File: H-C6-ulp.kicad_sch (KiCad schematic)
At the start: 66 parts, among them J1 USB_C_Receptacle_USB2.0, J2 AFC24-S24FIC-00, J3 SM02B-SRSS-TB(LF)(SN), J4 SM04B-SRSS-TB_LF__SN_, Q1 Si1308, Q2 Si2301CDS, U1 ESP32-C6, U2 SGM6029CYG/TR, U3 TP4057-42-SOT26-R, X1 Crystal 40 Mhz 10ppm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

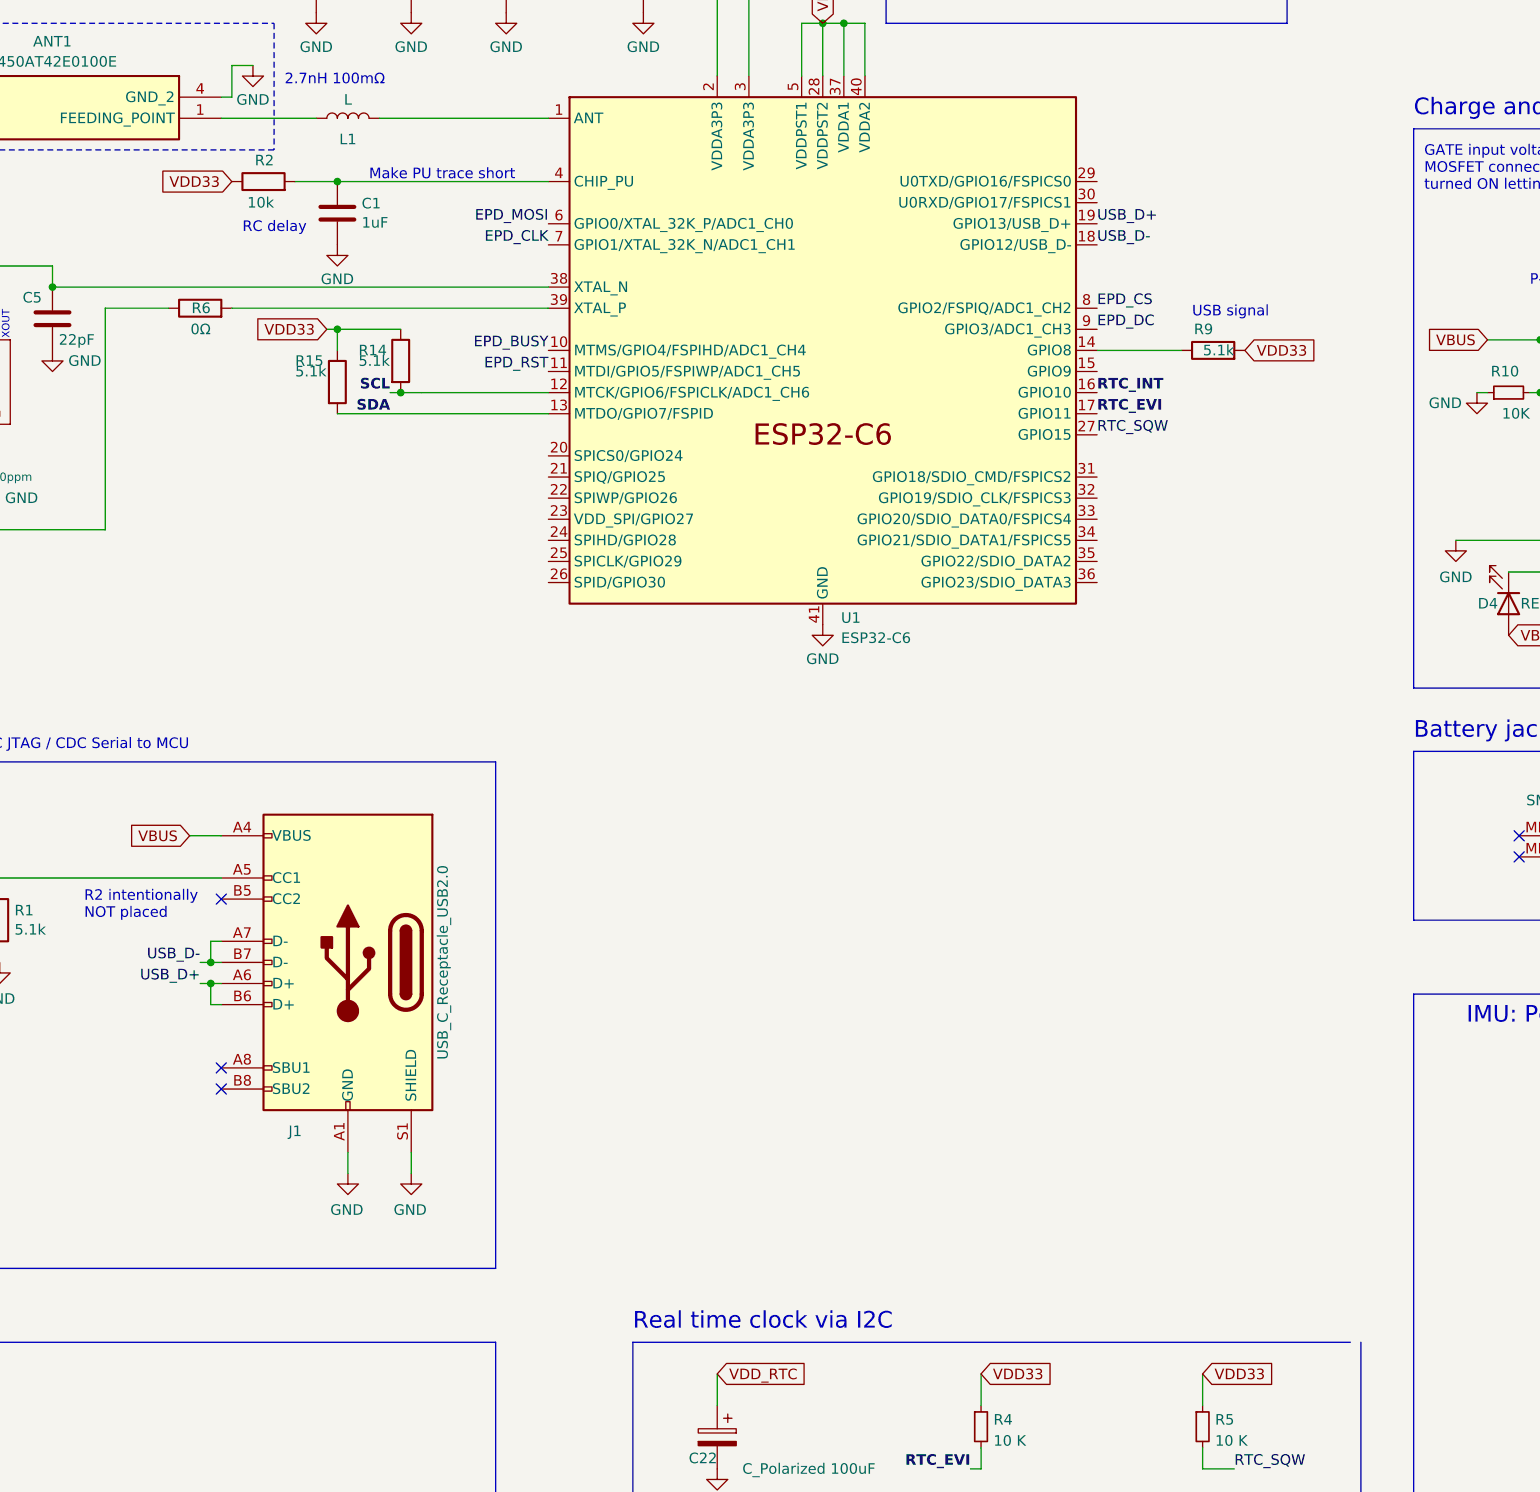
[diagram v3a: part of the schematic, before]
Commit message: Add BOOT & RST switches
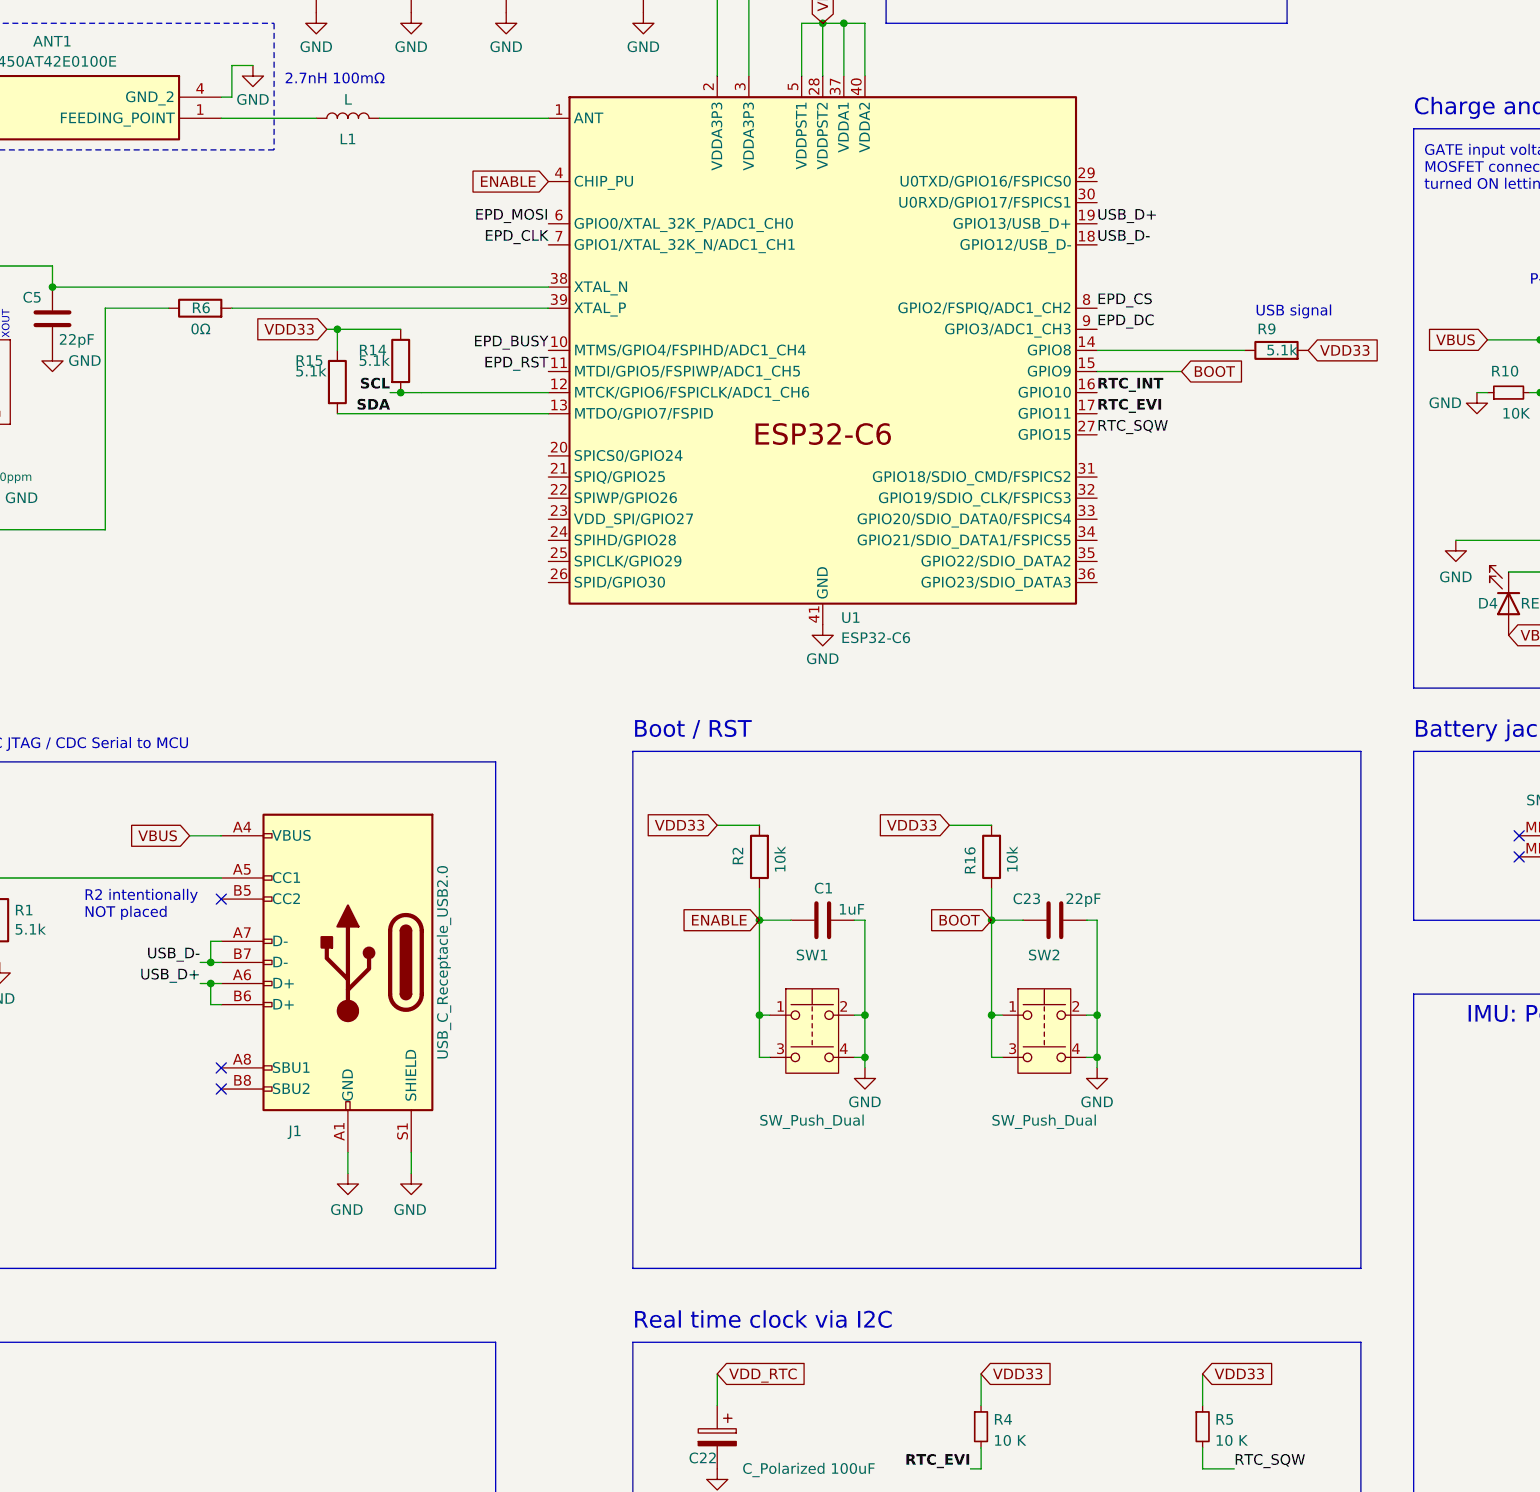
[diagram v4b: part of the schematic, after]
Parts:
- added C23: 22pF, Capacitor_SMD:C_0603_1608Metric, symbol Device:C
- added R16: 10k, Resistor_SMD:R_0603_1608Metric, symbol Device:R
- added SW1, SW2: SW_Push_Dual, footprints:switch_SKSVCCE010, symbol Switch:SW_Push_Dual
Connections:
- net GND: now also C23.2, SW1.2, SW1.4, SW2.2, SW2.4
- net VDD33: now also R2.2, R16.2; no longer R2.1
- net ENABLE: now reaches C1.2, U1.4 (CHIP_PU)
- net ENABLE: now also R2.1, SW1.1, SW1.3; no longer R2.2
- net BOOT: now reaches U1.15 (GPIO9)
- net BOOT: now also C23.1, R16.1, SW2.1, SW2.3
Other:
- note added: "Boot / RST"
- note removed: "Make PU trace short"
- note removed: "RC delay"
- moved on the sheet: R9

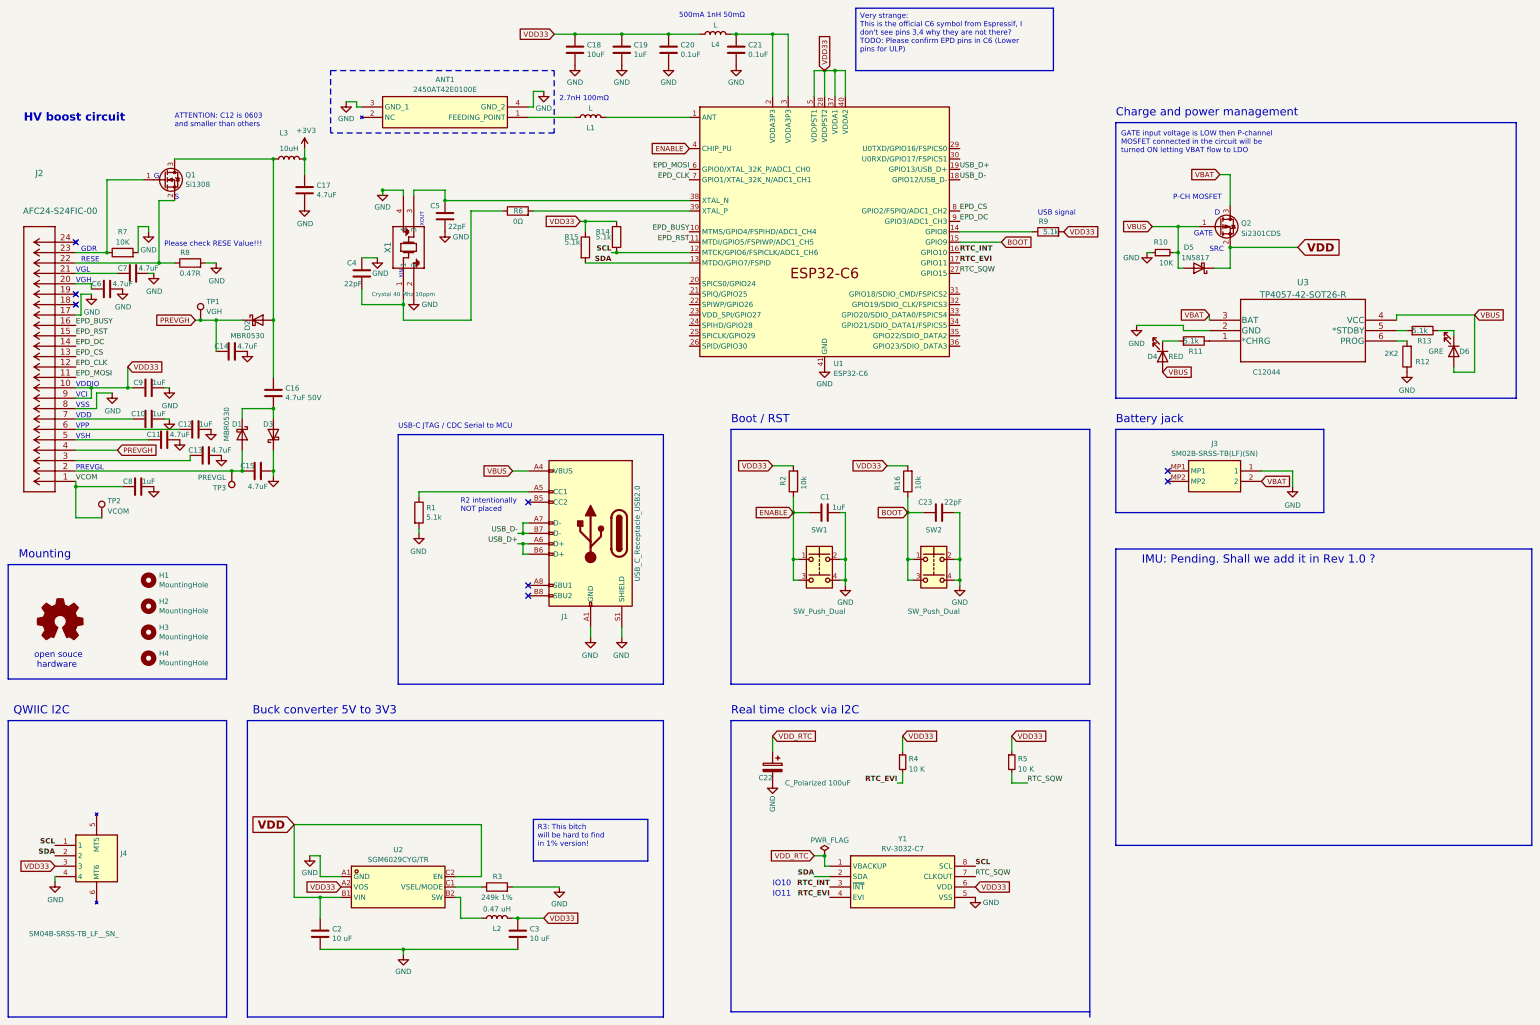
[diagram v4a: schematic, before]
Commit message: 3 buttons, a bit risky routing
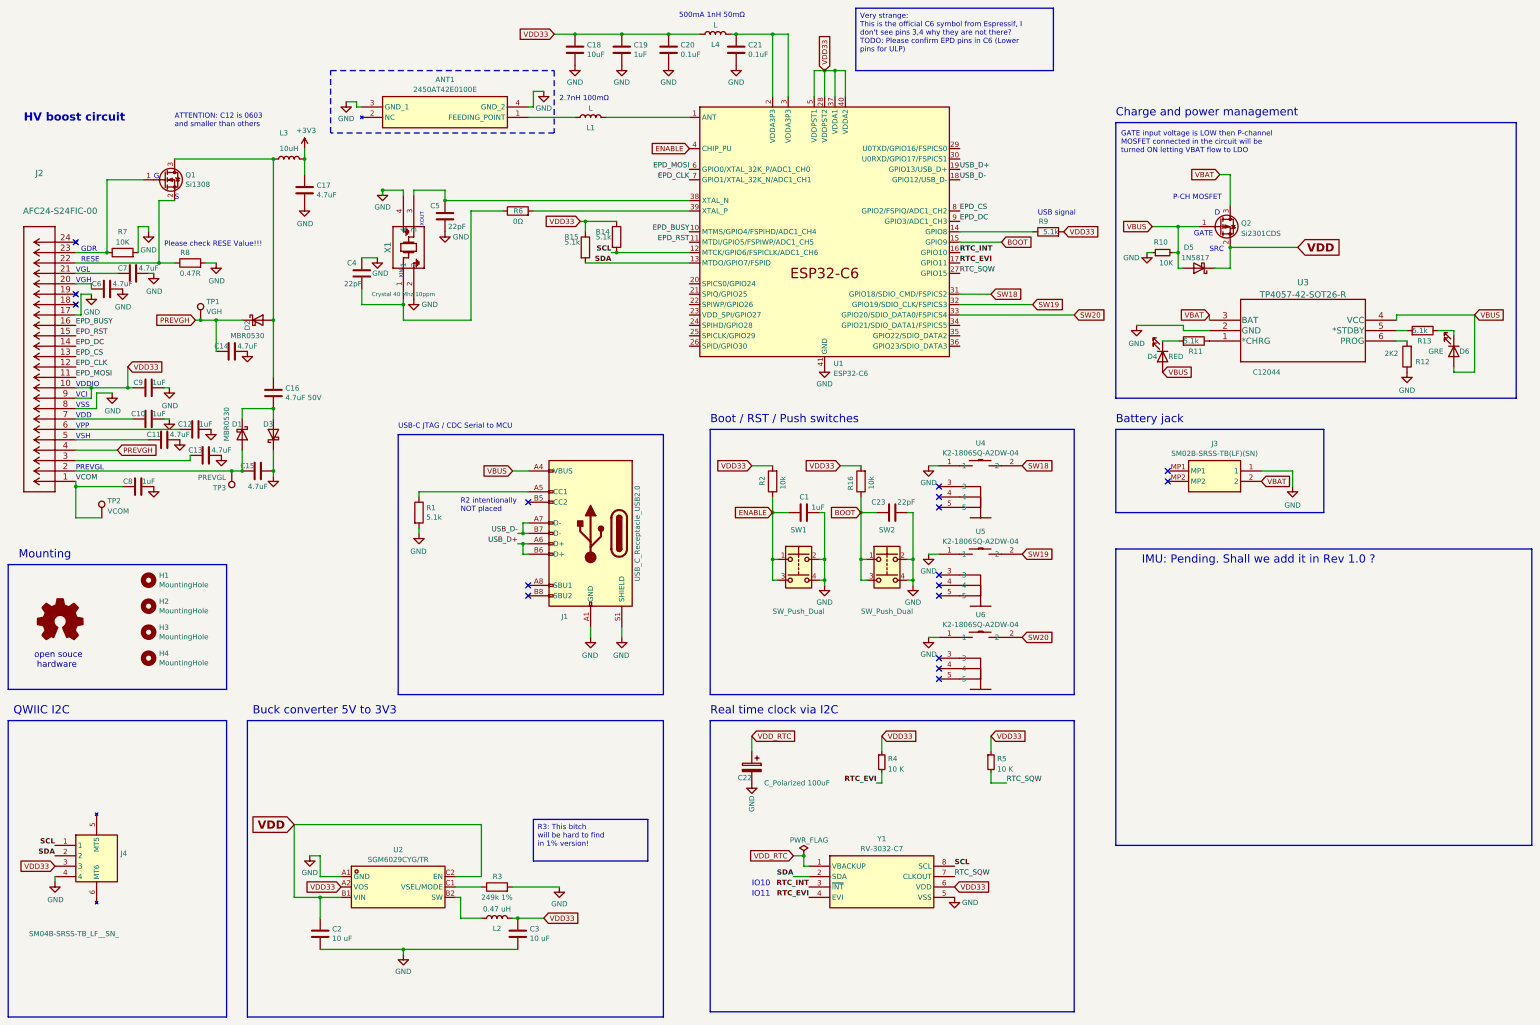
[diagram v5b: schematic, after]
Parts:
- added U4, U5, U6: K2-1806SQ-A2DW-04, footprints:KEY-SMD_K2-1806SQ-A3DW-04, symbol easyeda:K2-1806SQ-A2DW-04
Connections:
- net GND: now also U4.1, U5.1, U6.1
- net SW18: now reaches U1.31 (GPIO18/SDIO_CMD/FSPICS2)
- net SW18: now also U4.2
- net SW19: now reaches U1.32 (GPIO19/SDIO_CLK/FSPICS3)
- net SW19: now also U5.2
- net SW20: now reaches U1.33 (GPIO20/SDIO_DATA0/FSPICS4)
- net SW20: now also U6.2
- no-connect marks 8 -> 17
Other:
- note added: "Boot / RST / Push switches"
- note removed: "Boot / RST"
- moved on the sheet: C1, C22, C23, R16, R2, R4, R5, SW1, SW2, Y1

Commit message: Add Readme
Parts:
- U1: LCSC (none) -> C5364646
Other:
- note removed: "ATTENTION: C12 is 0603 and smaller than others"
- note removed: "Please check RESE Value!!!"
- moved on the sheet: C17, C4, C5, L3, R6, X1

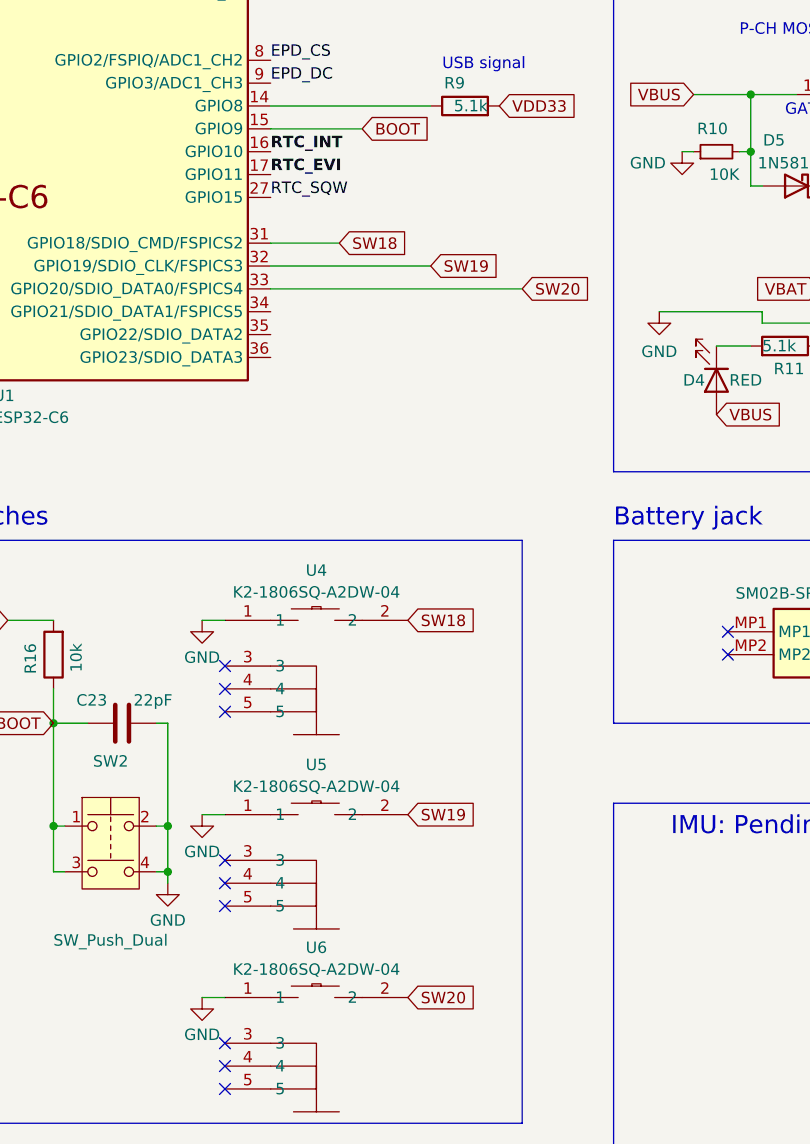
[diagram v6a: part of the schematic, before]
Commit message: Add pull-ups
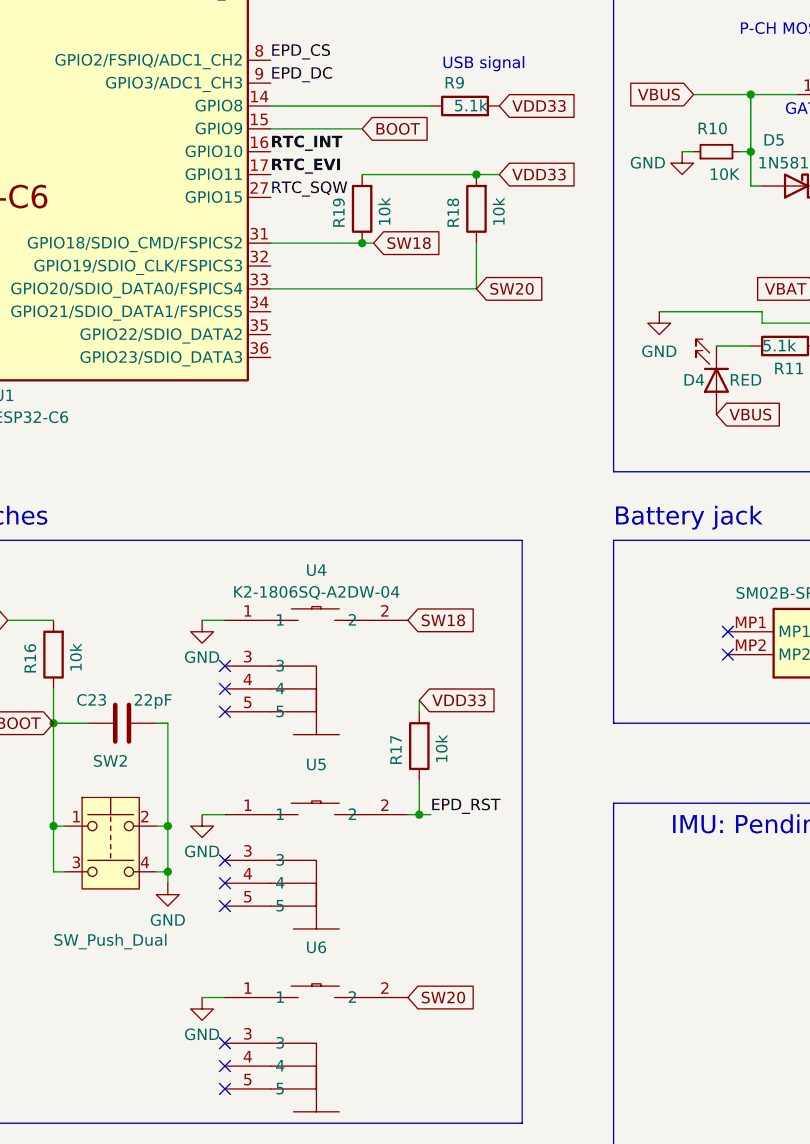
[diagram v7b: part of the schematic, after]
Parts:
- added R17, R18, R19: 10k, Resistor_SMD:R_0402_1005Metric, symbol Device:R
- R16, R2: footprint Resistor_SMD:R_0603_1608Metric -> Resistor_SMD:R_0402_1005Metric; LCSC C5123581 -> C4322213
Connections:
- net EPD_RST: now also U5.2, R17.1
- net SW18: now also R19.1
- net SW20: now also R18.1
- net VDD33: now also R17.2, R18.2, R19.2
- net SW19: no longer names the net of U1.32 (GPIO19/SDIO_CLK/FSPICS3)
- net SW19: no longer U5.2
